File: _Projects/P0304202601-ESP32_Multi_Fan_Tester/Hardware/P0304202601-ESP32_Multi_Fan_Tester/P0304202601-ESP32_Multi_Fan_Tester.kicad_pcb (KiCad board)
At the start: 4 copper layers, 92.5 x 82 mm, 71 parts, among them CN1 KHS4B-PH-SM4-TB(LF)(SN), CN2 KHS4B-PH-SM4-TB(LF)(SN), CN3 KJ694108301002, CN4 KTBL002B-350-04GR-2OR, CN5 KH470533000, IC1 PMAP63205WU-7, IC2 ESP32-WROOM-32UE-N16, IC3 PMAP63203WU-7, J1 KH22-28-5021, J2 KH22-28-5021, J3 KH22-28-5021, J4 KH68001-406HLF, Q1 SSM3K2615R,LF, Q2 SSM3K2615R,LF, Q3 SSM3K2615R,LF

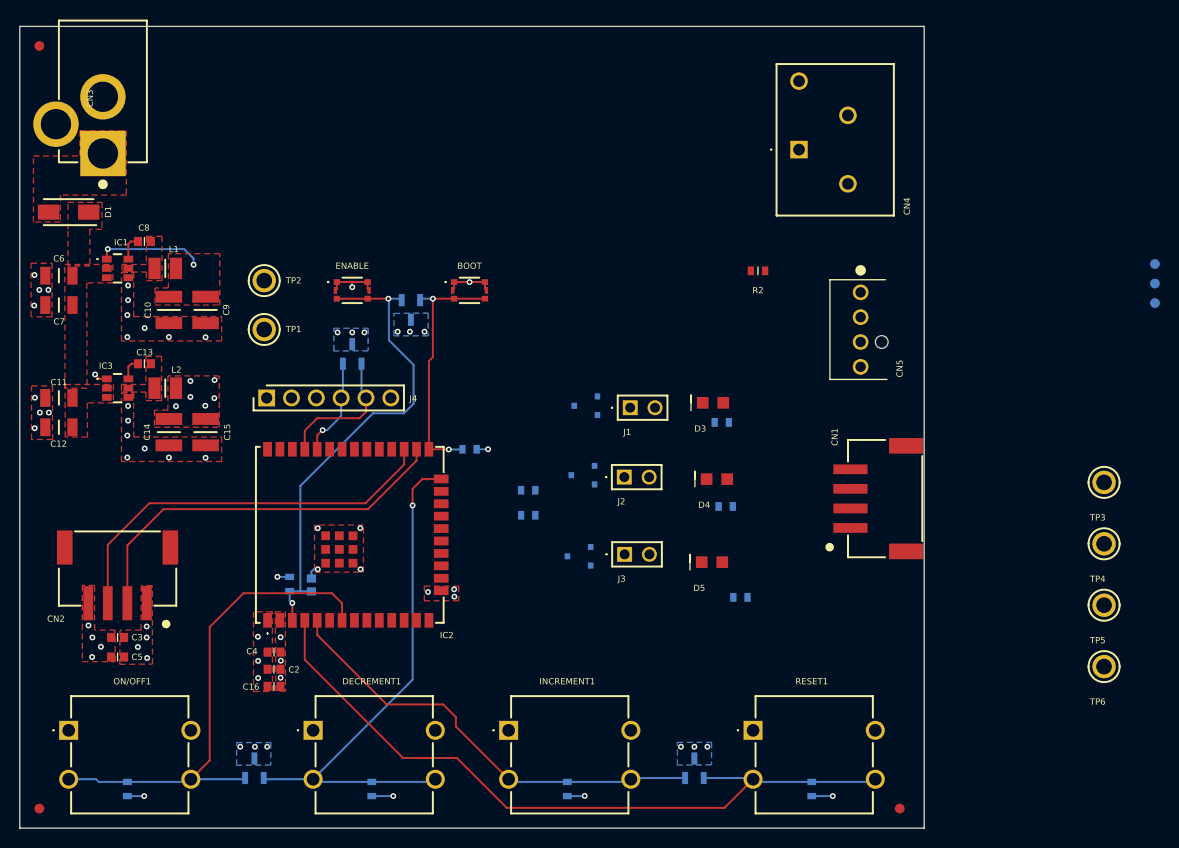
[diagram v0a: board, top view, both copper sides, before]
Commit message: Updated files from video stream.
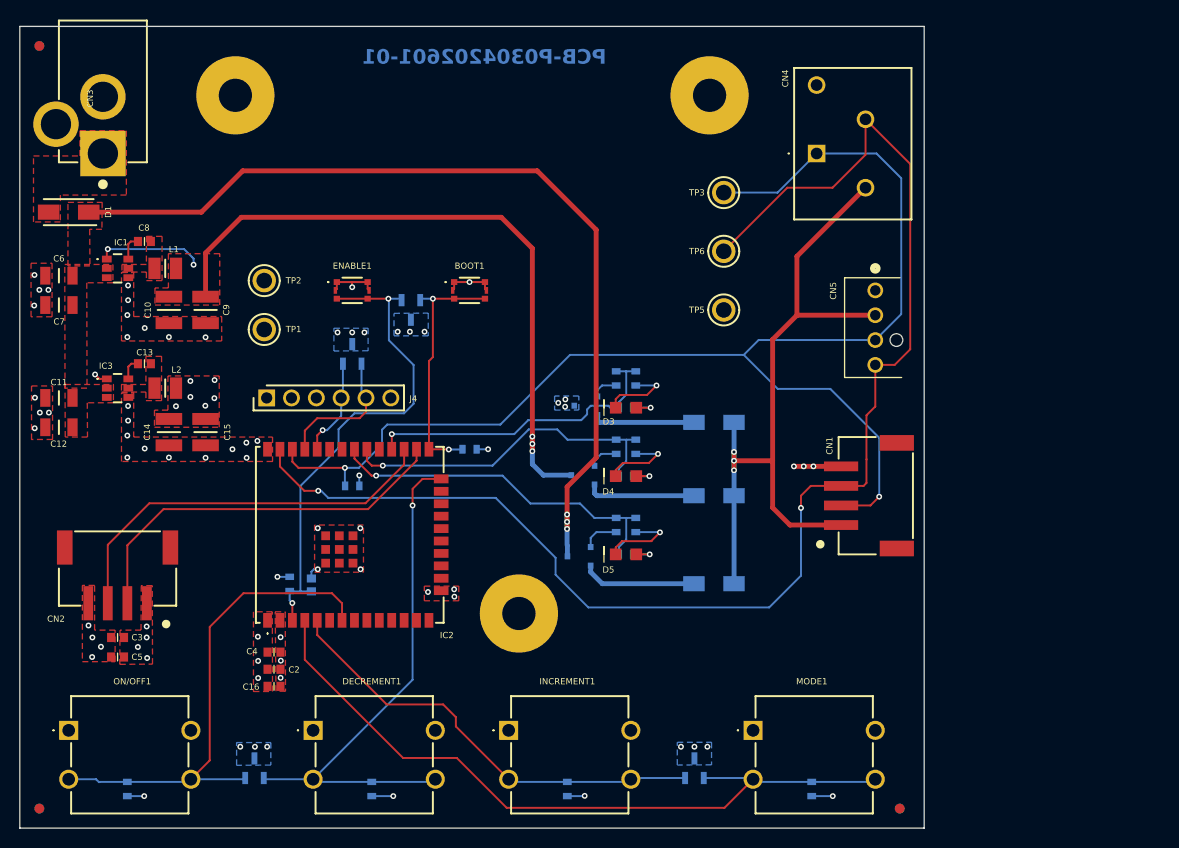
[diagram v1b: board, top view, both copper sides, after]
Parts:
- removed J1, J2, J3: KH22-28-5021, CONNECTORS:2x1HDR2.54mm
- removed TP4: TP5010, CONNECTORS:5010
- added D10: DSSS26SHE3_B_H, COMPONENTS:SMA, B.Cu at (161.1, 116.0)
- added D11: DSSS26SHE3_B_H, COMPONENTS:SMA, B.Cu at (161.1, 125.0)
- added D9: DSSS26SHE3_B_H, COMPONENTS:SMA, B.Cu at (161.1, 108.5)
- added MH1: ~, HARDWARE:M3MountingHole, F.Cu at (112.1, 75.0)
- added MH2: ~, HARDWARE:M3MountingHole, F.Cu at (160.6, 75.0)
- added MH3: ~, HARDWARE:M3MountingHole, F.Cu at (141.1, 128.0)
- added R13: RC060310K2075AAA, COMPONENTS:RES-0603, B.Cu at (153.1, 111.0)
- added R14: 100Ω, COMPONENTS:RES-0603, B.Cu at (151.1, 111.0)
- added R15: RC060310K2075AAA, COMPONENTS:RES-0603, B.Cu at (153.1, 119.0)
- added R16: 100Ω, COMPONENTS:RES-0603, B.Cu at (151.1, 119.0)
- R2: moved to B.Cu
- R5: value RC0603510075AAA -> RC0603330075AAA
- R6: value RC06031K0075AAA -> RC0603330075AAA
- moved FID4 127.0 mm to (92.1, 148.0)
- moved FID6 117.1 mm to (92.1, 70.0)
- moved FID5 59.7 mm to (180.1, 148.0)
- moved TP6 57.6 mm to (162.1, 91.0)
- moved TP5 49.2 mm to (162.1, 97.0)
- moved TP3 48.9 mm to (162.1, 85.0)
- moved R2 47.0 mm to (124.1, 115.0), turned to 180 degrees
- moved R12 17.8 mm to (153.1, 104.0), turned to -90 degrees
- moved R11 14.6 mm to (151.1, 104.0), turned to -90 degrees
- moved R6 12.5 mm to (152.1, 122.0), turned to 0 degrees
- moved R5 10.7 mm to (152.1, 114.0), turned to 0 degrees
- moved R4 9.91 mm to (152.1, 107.0), turned to 0 degrees
- moved D4 9.30 mm to (152.1, 114.0)
- moved D3 8.91 mm to (152.1, 107.0)
- moved D5 8.84 mm to (152.1, 122.0)
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- renumbered BOOT to BOOT1, ENABLE to ENABLE1, RESET1 to MODE1
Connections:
- net /ESP32/RESET_SW renamed /ESP32/MODE_SW
- IC2 pad 28: FAN_PWR_CNTROL -> 3V3_FAN
- IC2 pad 30: unconnected-(IC2-IO18-Pad30) -> 5V0_FAN
- IC2 pad 31: unconnected-(IC2-IO19-Pad31) -> 12V0_FAN
- Q1 pad 1: /Fan Connections/PWR_CNTRL -> Net-(Q1-G)
- Q2 pad 1: /Fan Connections/PWR_CNTRL -> Net-(Q2-G)
- Q3 pad 1: /Fan Connections/PWR_CNTRL -> Net-(Q3-G)
- R11 pad 1: FAN_PWR_CNTROL -> 3V3_FAN
- R11 pad 2: /Fan Connections/PWR_CNTRL -> Net-(Q1-G)
- R12 pad 1: FAN_PWR_CNTROL -> 3V3_FAN
- R4 pad 1: /Fan Connections/FAN_VCC -> 3V3_FAN
- R5 pad 1: /Fan Connections/FAN_VCC -> 5V0_FAN
- R6 pad 1: /Fan Connections/FAN_VCC -> 12V0_FAN
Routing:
- net FAN_PWM: track 0.00 -> 143.1 mm, vias 0 -> 2
- net FAN_TACH: track 0.00 -> 135.5 mm, vias 0 -> 2
- net +12V: track 0.00 -> 92.3 mm, vias 0 -> 3
- net /Fan Connections/FAN_VCC: track 0.00 -> 74.7 mm, vias 0 -> 3
- net +5V: track 10.9 -> 79.6 mm, vias 2 -> 5
- net 12V0_FAN: track 0.00 -> 36.3 mm, vias 0 -> 1
- net 5V0_FAN: track 0.00 -> 34.9 mm, vias 0 -> 1
- net 3V3_FAN: track 0.00 -> 32.4 mm, vias 0 -> 1
- net GND: track 19.8 -> 48.6 mm, vias 54 -> 64
- net Net-(D11-A): track 0.00 -> 11.7 mm
- net Net-(D10-A): track 0.00 -> 11.2 mm
- net Net-(D9-A): track 0.00 -> 10.5 mm
- net Net-(Q3-G): track 0.00 -> 3.79 mm
- net Net-(D3-A): track 0.00 -> 3.28 mm, vias 0 -> 1
- net Net-(D5-A): track 0.00 -> 3.08 mm, vias 0 -> 1
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- added copper zone on B.Cu, net +3.3V
- added copper zone on In2.Cu, net +3.3V
- added copper zone on In1.Cu, net GND
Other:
- board text added: "PCB-P0304202601-01"
